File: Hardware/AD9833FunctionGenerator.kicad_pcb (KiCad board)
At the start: 2 copper layers, 161.3 x 114.3 mm, 48 parts, among them U1 LM7805_TO220

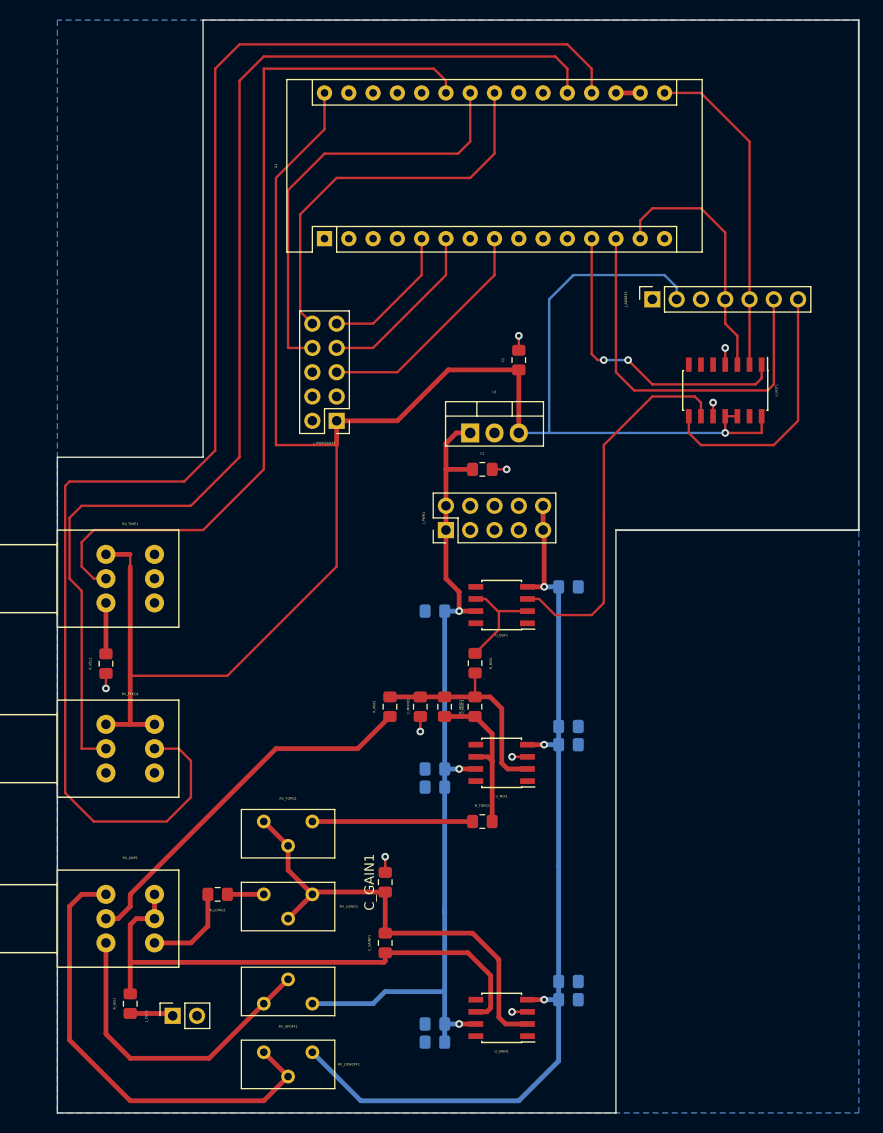
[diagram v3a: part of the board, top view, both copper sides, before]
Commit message: updated HW
- Added separate analog and digital ground to prevent output signal ripple/jitter
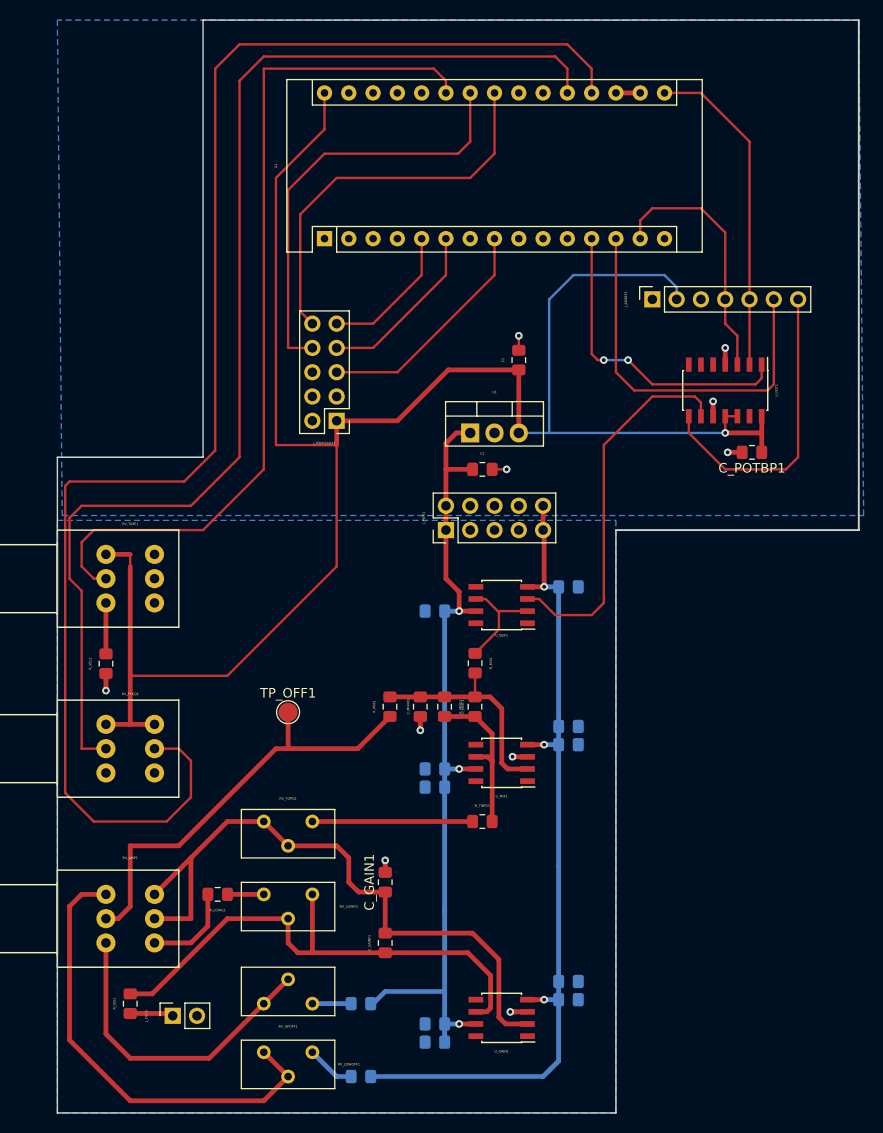
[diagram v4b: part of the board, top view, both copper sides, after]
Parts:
- added C_POTBP1: 100nF, Capacitor_SMD:C_0805_2012Metric_Pad1.15x1.40mm_HandSolder, F.Cu at (192.0, 80.8)
- added R_HIOFF1: 220R, Resistor_SMD:R_0805_2012Metric_Pad1.15x1.40mm_HandSolder, B.Cu at (151.1, 138.4)
- added R_LOFF1: 220R, Resistor_SMD:R_0805_2012Metric_Pad1.15x1.40mm_HandSolder, B.Cu at (151.1, 146.1)
- added TP_OFF1: TestPoint, TestPoint:TestPoint_Pad_D2.0mm, F.Cu at (143.5, 108.0)
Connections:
- C_BUFBP1 pad 2: /GND -> /AGND
- C_BUFBP2 pad 2: /GND -> /AGND
- C_GAIN1 pad 2: /GND -> /AGND
- C_GAINBP1 pad 2: /GND -> /AGND
- C_GAINBP2 pad 2: /GND -> /AGND
- C_GAINBP3 pad 2: /GND -> /AGND
- C_GAINBP4 pad 2: /GND -> /AGND
- C_MIXBP1 pad 2: /GND -> /AGND
- C_MIXBP2 pad 2: /GND -> /AGND
- C_MIXBP3 pad 2: /GND -> /AGND
- C_MIXBP4 pad 2: /GND -> /AGND
- C_MIXIN1 pad 2: /GND -> /AGND
- J_OUT1 pad 2: /GND -> /AGND
- J_PWR1 pad 3: /GND -> /AGND
- J_PWR1 pad 5: /GND -> /AGND
- J_PWR1 pad 7: /GND -> /AGND
- RV_AMP1 pad 5: Net-(C_GAINF1-Pad1) -> Net-(C_GAIN1-Pad1)
- RV_AMP1 pad 6: Net-(C_GAINF1-Pad1) -> Net-(C_GAIN1-Pad1)
- RV_FREQ1 pad 1: /GND -> /AGND
- RV_FREQ1 pad 4: /GND -> /AGND
- RV_LOWG1 pad 1: Net-(C_GAIN1-Pad1) -> Net-(C_GAINF1-Pad1)
- RV_LOWG1 pad 2: Net-(C_GAIN1-Pad1) -> Net-(C_GAINF1-Pad1)
- RV_LOWOFF1 pad 1: /-12V -> Net-(RV_LOWOFF1-Pad1)
- RV_UPOFF1 pad 3: /+12V -> Net-(RV_UPOFF1-Pad3)
- R_VEL1 pad 1: /GND -> /AGND
- U_GAIN1 pad 3: /GND -> /AGND
- U_MIX1 pad 3: /GND -> /AGND
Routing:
- net Net-(C_GAIN1-Pad1): track 47.4 -> 68.4 mm
- net /-12V: track 97.5 -> 88.0 mm
- net /AGND: track 0.00 -> 7.88 mm, vias 0 -> 5
- net /5V: track 200.4 -> 208.0 mm
- net Net-(RV_AMP1-Pad2): track 39.2 -> 46.0 mm
- net /GND: track 14.2 -> 7.85 mm, vias 9 -> 5
- net /+12V: track 93.7 -> 87.4 mm
- net Net-(RV_LOWOFF1-Pad1): track 0.00 -> 5.11 mm
- net /DDS_SIG: track 27.5 -> 31.8 mm
- net Net-(RV_UPOFF1-Pad3): track 0.00 -> 4.05 mm
- net Net-(C_GAINF1-Pad1): track 57.4 -> 56.1 mm
- added copper zone on B.Cu, net /AGND

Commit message: board rev b
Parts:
- removed C_BUFBP1, C_BUFBP2: 100nF, Capacitor_SMD:C_0805_2012Metric_Pad1.15x1.40mm_HandSolder
- removed C_GAINBP1, C_GAINBP4, C_MIXBP1: 2.2uF TANT., Capacitor_SMD:C_0805_2012Metric_Pad1.15x1.40mm_HandSolder
- removed C_GAINBP2, C_GAINBP3, C_MIXBP2, C_MIXBP3: 10nF, Capacitor_SMD:C_0805_2012Metric_Pad1.15x1.40mm_HandSolder
- removed C_GAINF1, C_MIXF1, C_MIXIN1: ?, Capacitor_SMD:C_0805_2012Metric_Pad1.15x1.40mm_HandSolder
- removed C_MIXBP4: 2.2pF TANT., Capacitor_SMD:C_0805_2012Metric_Pad1.15x1.40mm_HandSolder
- removed RV_LOWG1: 100R, Potentiometer_THT:Potentiometer_Bourns_3296Y_Vertical
- removed RV_TOPG1: 10K, Potentiometer_THT:Potentiometer_Bourns_3296Y_Vertical
- removed R_LOWG1: 120R, Resistor_SMD:R_0805_2012Metric_Pad1.15x1.40mm_HandSolder
- removed R_MIXF1: 10K, Resistor_SMD:R_0805_2012Metric_Pad1.15x1.40mm_HandSolder
- removed R_TOPG1: 330R, Resistor_SMD:R_0805_2012Metric_Pad1.15x1.40mm_HandSolder
- removed U_BUF1: TL071, Package_SO:SOIC-8_3.9x4.9mm_P1.27mm
- removed U_GAIN1, U_MIX1: LM7171, Package_SO:SOIC-8_3.9x4.9mm_P1.27mm
- added C_BUFFBP1: 100nF, Capacitor_SMD:C_0805_2012Metric_Pad1.15x1.40mm_HandSolder, B.Cu at (148.6, 138.1)
- added C_BUFFBP2: 100nF, Capacitor_SMD:C_0805_2012Metric_Pad1.15x1.40mm_HandSolder, B.Cu at (158.1, 104.2)
- added RF1: 1k, Resistor_SMD:R_0805_2012Metric_Pad1.15x1.40mm_HandSolder, F.Cu at (153.7, 114.9)
- added RF2: 8K2, Resistor_SMD:R_0805_2012Metric_Pad1.15x1.40mm_HandSolder, F.Cu at (129.5, 137.2)
- added RG1: 1k, Resistor_SMD:R_0805_2012Metric_Pad1.15x1.40mm_HandSolder, F.Cu at (159.4, 110.9)
- added ROFF1: 1K, Resistor_SMD:R_0805_2012Metric_Pad1.15x1.40mm_HandSolder, F.Cu at (195.6, 69.1)
- added ROFF2: 1K, Resistor_SMD:R_0805_2012Metric_Pad1.15x1.40mm_HandSolder, F.Cu at (168.7, 89.4)
- added R_MIX3: 1K, Resistor_SMD:R_0805_2012Metric_Pad1.15x1.40mm_HandSolder, F.Cu at (139.9, 115.6)
- added UBUFF1: LT1227, Package_SO:SOIC-8_3.9x4.9mm_P1.27mm, F.Cu at (153.7, 109.2)
- added UMIX1: LT1227, Package_SO:SOIC-8_3.9x4.9mm_P1.27mm, F.Cu at (153.7, 134.6)
- C_POTBP1, U_POT1: moved to B.Cu
- R_HIOFF1, R_LOFF1: value 220R -> 1K; moved to F.Cu
- R_MIX1, R_MIX2: value 10K -> 1K
- moved R_LOFF1 45.4 mm to (171.4, 105.4), turned to 0 degrees
- moved RV_LOWOFF1 39.6 mm to (172.7, 114.3), turned to 270 degrees
- moved RV_UPOFF1 31.8 mm to (172.7, 139.7), turned to 270 degrees
- moved C_POTBP1 29.7 mm to (162.6, 84.3), turned to 270 degrees
- moved R_MIX1 29.0 mm to (135.9, 113.0), turned to 0 degrees
- moved U_POT1 23.8 mm to (169.2, 87.1), turned to 180 degrees
- moved R_HIOFF1 21.7 mm to (171.4, 130.8), turned to 0 degrees
- moved R_MIX2 20.0 mm to (135.9, 115.6), turned to 0 degrees
- moved J_AD9833 16.5 mm to (198.1, 64.8), turned to 270 degrees
- moved TP_OFF1 15.3 mm to (153.7, 96.5), turned to 180 degrees
- moved C2 14.7 mm to (156.4, 80.7), turned to 180 degrees
- moved C1 14.3 mm to (149.7, 80.7)
- moved C_GAIN1 12.1 mm to (162.6, 134.0), turned to 0 degrees
- moved J_PWR1 11.4 mm to (148.6, 88.9)
- moved J_OUT1 6.25 mm to (137.2, 137.2)
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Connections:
- RV_AMP1 pad 4: Net-(RV_AMP1-Pad4) -> Net-(C_GAIN1-Pad1)
- RV_AMP1 pad 5: Net-(C_GAIN1-Pad1) -> Net-(RV_AMP1-Pad5)
- RV_AMP1 pad 6: Net-(C_GAIN1-Pad1) -> Net-(RV_AMP1-Pad5)
- RV_LOWOFF1 pad 1: Net-(RV_LOWOFF1-Pad1) -> Net-(RV_AMP1-Pad3)
- RV_LOWOFF1 pad 3: Net-(RV_AMP1-Pad3) -> Net-(RV_LOWOFF1-Pad3)
- R_LOFF1 pad 2: Net-(RV_LOWOFF1-Pad1) -> Net-(RV_LOWOFF1-Pad3)
- R_MIX1 pad 2: Net-(C_MIXF1-Pad2) -> Net-(RV_AMP1-Pad5)
- R_MIX2 pad 2: Net-(C_MIXF1-Pad2) -> Net-(RV_AMP1-Pad5)
- U_POT1 pad 10: /GND -> /AGND
- U_POT1 pad 5: (no net) -> Net-(ROFF2-Pad1)
- U_POT1 pad 6: (no net) -> /OFFSETADJUST
- U_POT1 pad 7: (no net) -> Net-(ROFF1-Pad1)
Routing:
- net Net-(RV_AMP1-Pad3): track 48.4 -> 111.9 mm
- net /OFFSETADJUST: track 0.00 -> 54.9 mm, vias 0 -> 1
- net Net-(ROFF1-Pad1): track 0.00 -> 41.6 mm, vias 0 -> 1
- net Net-(RV_AMP1-Pad1): track 33.0 -> 69.2 mm
- net Net-(C_GAIN1-Pad1): track 68.4 -> 37.4 mm
- net /DDS_CS: track 40.4 -> 12.5 mm
- net Net-(RF2-Pad1): track 56.1 -> 30.6 mm
- net /+12V: track 87.4 -> 112.3 mm, vias 3 -> 2
- net Net-(RV_AMP1-Pad5): track 0.00 -> 23.8 mm
- net Net-(C_MIXF1-Pad2): track 23.4 -> 0.00 mm
- net /MOSI: track 26.7 -> 49.0 mm
- net /-12V: track 88.0 -> 69.9 mm
- net /SCK: track 34.3 -> 51.9 mm
- net Net-(C_MIXF1-Pad1): track 16.8 -> 0.00 mm
- net Net-(RV_TOPG1-Pad1): track 16.8 -> 0.00 mm
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
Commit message: updated board layout
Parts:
- removed RV_TIME1: B10K, PTH901:PTH901
- removed UBUFF1, UMIX1: LT1227, Package_SO:SOIC-8_3.9x4.9mm_P1.27mm
- added CF2: 2pF, Capacitor_SMD:C_0805_2012Metric_Pad1.15x1.40mm_HandSolder, F.Cu at (145.5, 130.2)
- added C_BUFFBP3: 100nF, Capacitor_SMD:C_0805_2012Metric_Pad1.15x1.40mm_HandSolder, B.Cu at (159.4, 104.8)
- added C_BUFFBP4: 2.2uF, Capacitor_SMD:C_0805_2012Metric_Pad1.15x1.40mm_HandSolder, B.Cu at (161.9, 104.8)
- added C_MIXBP1: 2.2uF, Capacitor_SMD:C_0805_2012Metric_Pad1.15x1.40mm_HandSolder, B.Cu at (145.5, 137.2)
- added C_MIXBP2: 100nF, Capacitor_SMD:C_0805_2012Metric_Pad1.15x1.40mm_HandSolder, B.Cu at (148.6, 137.2)
- added C_MIXBP3: 100nF, Capacitor_SMD:C_0805_2012Metric_Pad1.15x1.40mm_HandSolder, B.Cu at (159.5, 128.8)
- added C_MIXBP4: 2.2uF, Capacitor_SMD:C_0805_2012Metric_Pad1.15x1.40mm_HandSolder, B.Cu at (161.5, 128.8)
- added REF**: MountingHole_2.2mm_M2_ISO7380, MountingHole:MountingHole_2.2mm_M2_ISO7380, F.Cu at (111.3, 77.2)
- added REF**: MountingHole_2.2mm_M2_ISO7380, MountingHole:MountingHole_2.2mm_M2_ISO7380, F.Cu at (75.7, 77.2)
- added REF**: MountingHole_2.2mm_M2_ISO7380, MountingHole:MountingHole_2.2mm_M2_ISO7380, F.Cu at (111.3, 38.1)
- added REF**: MountingHole_2.2mm_M2_ISO7380, MountingHole:MountingHole_2.2mm_M2_ISO7380, F.Cu at (75.7, 38.1)
- added RV_SPEED1: R_POT, PTD901:PTD90, F.Cu at (123.2, 134.6)
- added U_BUFF1: LM7171, Package_SO:SOIC-8_3.9x4.9mm_P1.27mm, F.Cu at (153.7, 109.2)
- added U_MIX1: LM7171, Package_SO:SOIC-8_3.9x4.9mm_P1.27mm, F.Cu at (153.7, 133.3)
- C_BUFFBP1: value 100nF -> 2.2uF
- RV_LOWOFF1, RV_UPOFF1: footprint Potentiometer_THT:Potentiometer_Bourns_3296Y_Vertical -> Potentiometer_THT:Potentiometer_Piher_PT-6-V_Vertical
- moved J_OLEDCONNECTOR1 45.9 mm to (89.8, 39.8), turned to 90 degrees
- moved R_VEL1 37.2 mm to (129.5, 139.7), turned to 180 degrees
- moved R_FUNC1 33.2 mm to (81.3, 64.5), turned to 270 degrees
- moved R_RANGE1 32.6 mm to (106.7, 64.5), turned to 270 degrees
- moved SW_FUNC1 32.3 mm to (77.7, 69.1)
- moved SW_MODE1 31.5 mm to (90.3, 69.1)
- moved J_AUX2MAIN2 31.3 mm to (106.2, 51.9)
- moved SW_RANGE1 30.5 mm to (102.6, 69.1)
- moved R_MODE1 24.6 mm to (87.4, 64.5), turned to 270 degrees
- moved C_BUFFBP1 24.5 mm to (146.1, 113.8)
- moved RV_FREQ1 17.8 mm to (127.0, 94.0)
- moved ROFF1 15.7 mm to (191.8, 84.3), turned to 0 degrees
- moved RF2 15.5 mm to (138.4, 124.5), turned to 180 degrees
- moved RV_LOWOFF1 15.5 mm to (188.0, 116.8), turned to 0 degrees
- moved RV_UPOFF1 15.5 mm to (188.0, 142.2), turned to 0 degrees
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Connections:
- C_BUFFBP2 pad 1: /-12V -> /+12V
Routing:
- net /AuxiliaryBoard/GND_AUX: track 95.5 -> 9.28 mm, vias 1 -> 0
- net /5V: track 219.3 -> 260.9 mm, vias 0 -> 1
- net /VEL1: track 85.4 -> 122.5 mm
- net Net-(RV_AMP1-Pad3): track 111.9 -> 145.7 mm
- net Net-(RV_AMP1-Pad1): track 69.2 -> 92.1 mm
- net Net-(RV_UPOFF1-Pad3): track 3.91 -> 25.4 mm
- net /AuxiliaryBoard/SDA_AUX: track 27.9 -> 7.06 mm
- net Net-(ROFF1-Pad1): track 41.6 -> 23.9 mm
- net /FREQ2: track 120.2 -> 102.6 mm
- net /AuxiliaryBoard/5V_AUX: track 61.2 -> 78.5 mm
- net /FREQ1: track 142.5 -> 125.7 mm
- net Net-(RV_LOWOFF1-Pad3): track 3.91 -> 20.0 mm
- net /AuxiliaryBoard/SCL_AUX: track 27.3 -> 11.8 mm
- net /AuxiliaryBoard/RANGEBTN_AUX: track 60.4 -> 47.8 mm
- net Net-(CF2-Pad1): track 30.6 -> 18.2 mm
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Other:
- board size 161.3 x 114.3 mm -> 129.5 x 114.3 mm
- board text added: "5V"

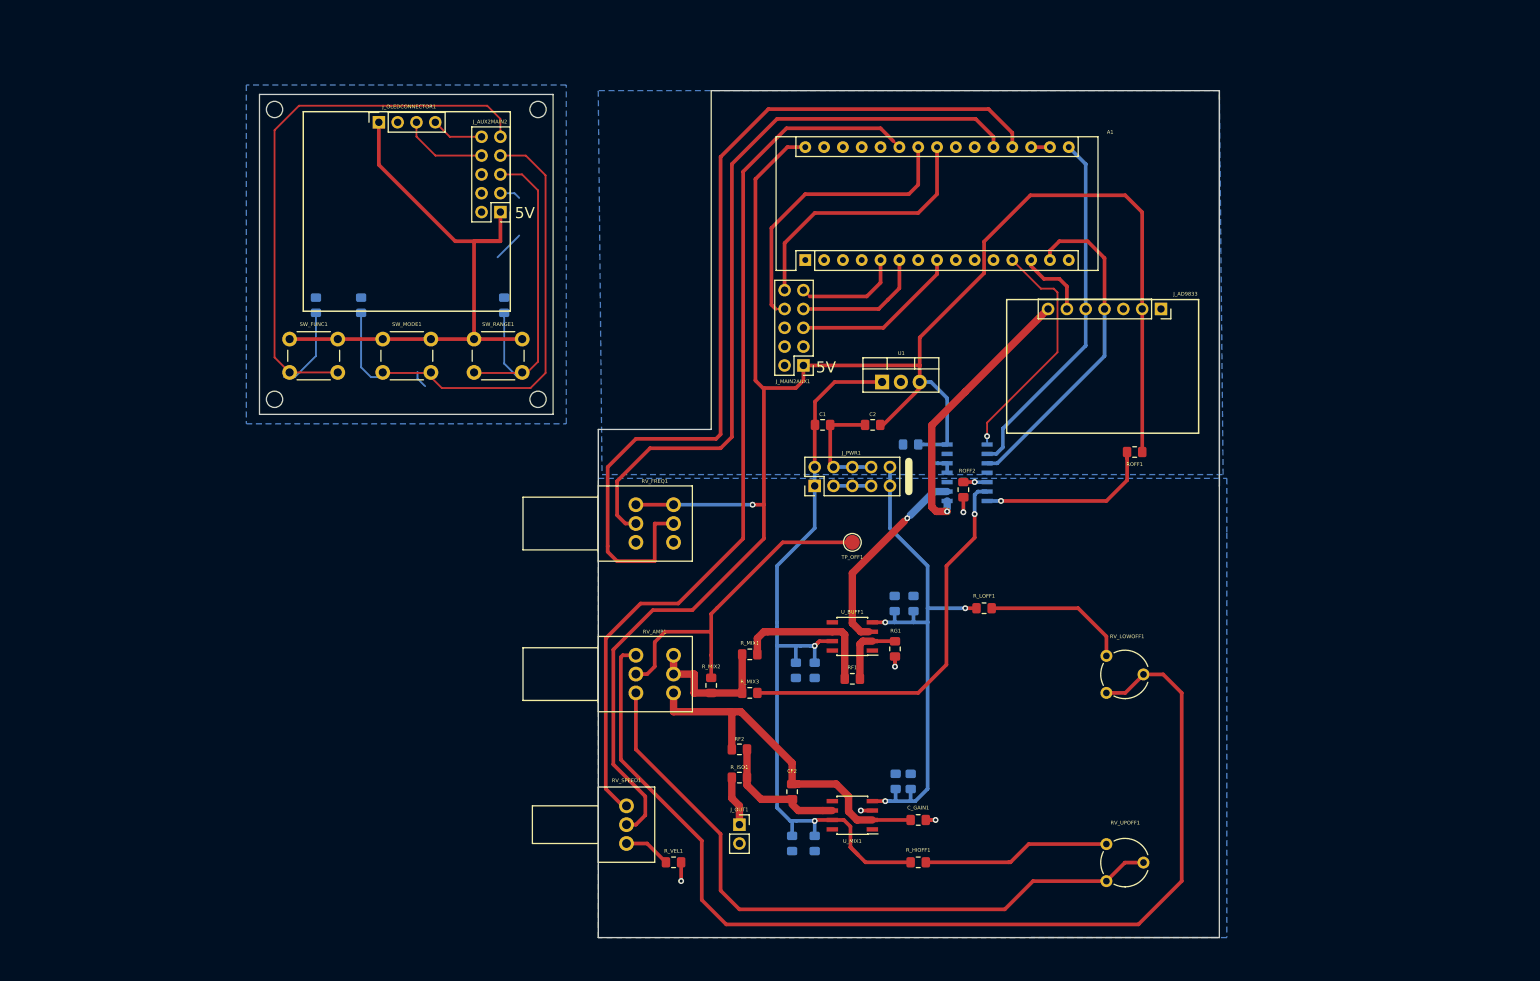
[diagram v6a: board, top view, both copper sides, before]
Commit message: updated hardware
- resized.relocated drill holes on aux board
- removed keep out areas for SPI/I2C clock signals
- Improved GND plane access for return signals
- rmoved traces from underneath MCP42050
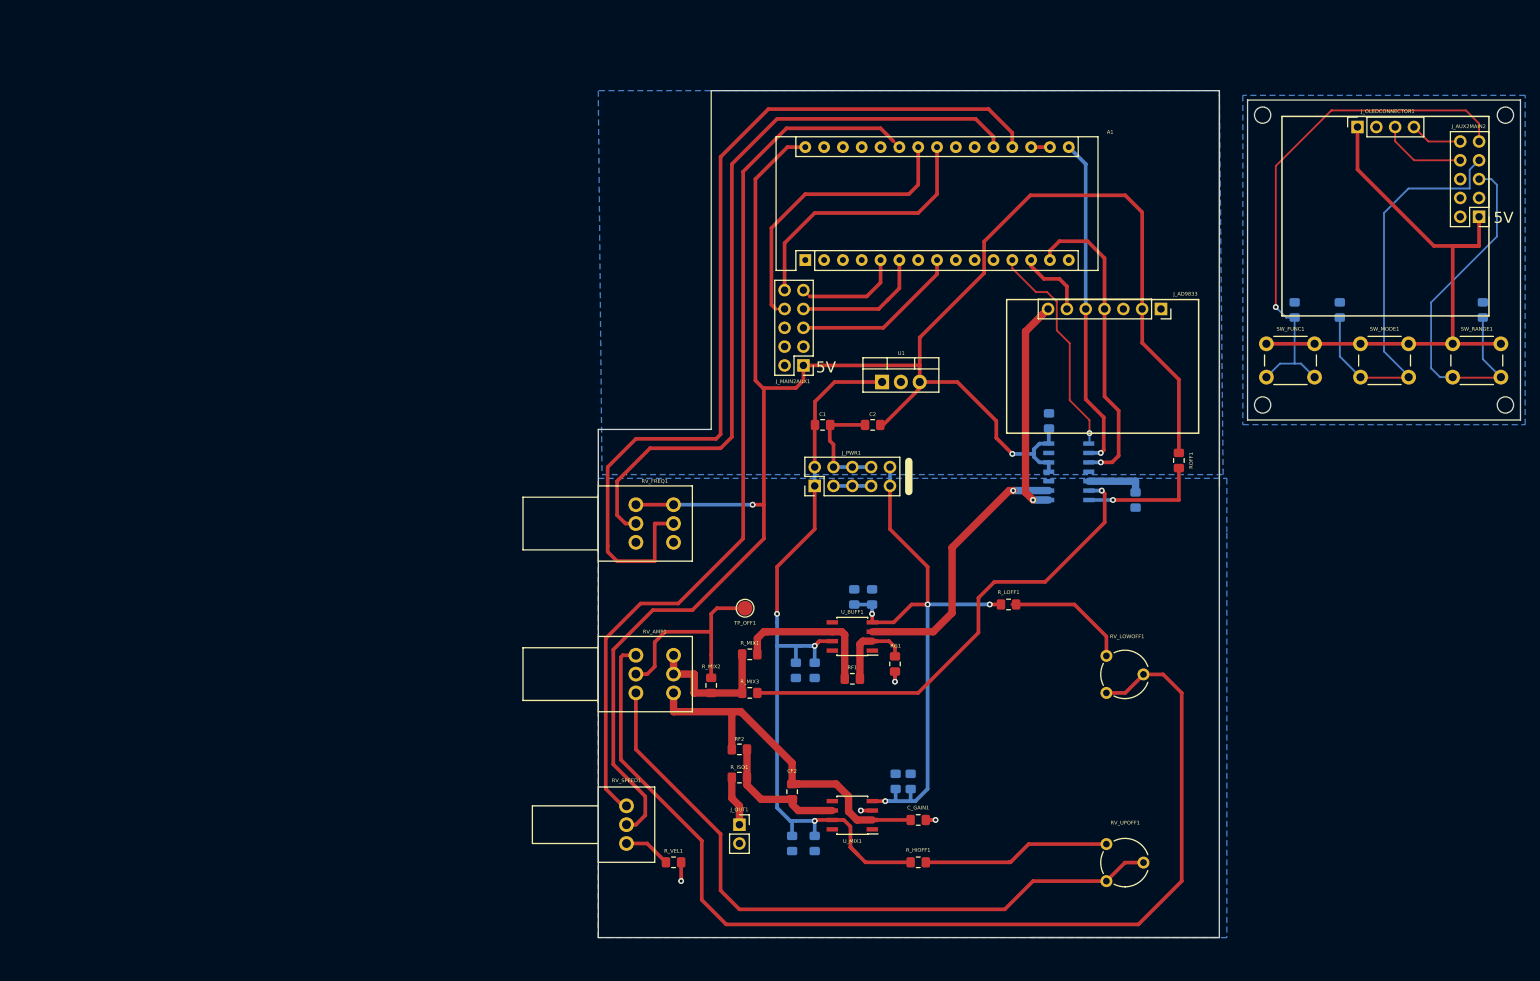
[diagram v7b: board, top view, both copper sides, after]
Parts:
- removed the REF** at (75.7, 77.2)
- removed the REF** at (111.3, 38.1)
- added REF**: MountingHole_2.2mm_M2_ISO7380, MountingHole:MountingHole_2.2mm_M2_ISO7380, F.Cu at (209.0, 78.0)
- added REF**: MountingHole_2.2mm_M2_ISO7380, MountingHole:MountingHole_2.2mm_M2_ISO7380, F.Cu at (241.8, 38.9)
- ROFF2: moved to B.Cu
- moved REF** 133.4 mm to (209.0, 38.9)
- moved J_AUX2MAIN2 132.1 mm to (238.3, 52.6)
- moved J_OLEDCONNECTOR1 132.1 mm to (221.8, 40.5)
- moved R_FUNC1 132.1 mm to (213.4, 65.2)
- moved R_MODE1 132.1 mm to (219.5, 65.2)
- moved R_RANGE1 132.1 mm to (238.8, 65.2)
- moved SW_RANGE1 132.1 mm to (234.7, 69.7)
- moved SW_MODE1 132.0 mm to (222.2, 69.7)
- moved SW_FUNC1 131.8 mm to (209.6, 69.7)
- moved REF** 130.6 mm to (241.8, 78.0)
- moved ROFF2 23.3 mm to (191.9, 90.8)
- moved C_POTBP1 18.9 mm to (180.2, 80.1), turned to 90 degrees
- moved TP_OFF1 17.0 mm to (139.2, 105.4)
- moved U_POT1 13.7 mm to (182.9, 87.0)
- moved C_BUFFBP4 8.05 mm to (153.9, 103.9)
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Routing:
- net Net-(RV_AMP1-Pad2): track 46.1 -> 28.0 mm
- net /AuxiliaryBoard/WAVEBTN_AUX: track 86.4 -> 70.1 mm, vias 0 -> 1
- net /AuxiliaryBoard/MODEBTN_AUX: track 68.6 -> 56.2 mm
- net /OFFSETADJUST: track 53.1 -> 65.0 mm
- net /5V: track 260.9 -> 272.4 mm, vias 1 -> 2
- net /DDS_REDUX: track 27.3 -> 37.3 mm
- net /AuxiliaryBoard/GND_AUX: track 9.28 -> 0.00 mm
- net Net-(ROFF1-Pad1): track 23.9 -> 16.5 mm
- net /DDS_SIG: track 37.0 -> 29.6 mm
- net /-12V: track 74.7 -> 80.8 mm, vias 3 -> 4
- net Net-(ROFF2-Pad1): track 3.21 -> 7.83 mm, vias 1 -> 0
- net /SCK: track 48.6 -> 45.0 mm, vias 0 -> 1
- net /MOSI: track 45.2 -> 42.0 mm, vias 0 -> 1
- net /AuxiliaryBoard/RANGEBTN_AUX: track 47.8 -> 50.8 mm
- net Net-(RV_LOWOFF1-Pad3): track 20.0 -> 17.1 mm
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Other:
- board size 129.5 x 114.3 mm -> 124.5 x 114.3 mm
